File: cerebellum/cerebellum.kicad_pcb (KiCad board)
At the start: 4 copper layers, 91.5 x 52 mm, 89 parts, among them J1 Power_IN, J10 Arm_R, J11 Light, J2 Power_Back, J3 GD_LINK, J4 GD_LINK, J5 Head, J7 Leg_L, J8 Leg_R, J9 Arm_L, Q1 AP2300, Q2 FH1404G6, Q3 FH1404G6, Q4 FH1404G6, U1 GD32F405VGHx, U2 TPS5430DDAR, U3 BMI088, U4 TCAN4550RGYRQ1, U5 ICP-20100, Y1 8M, Y2 40M

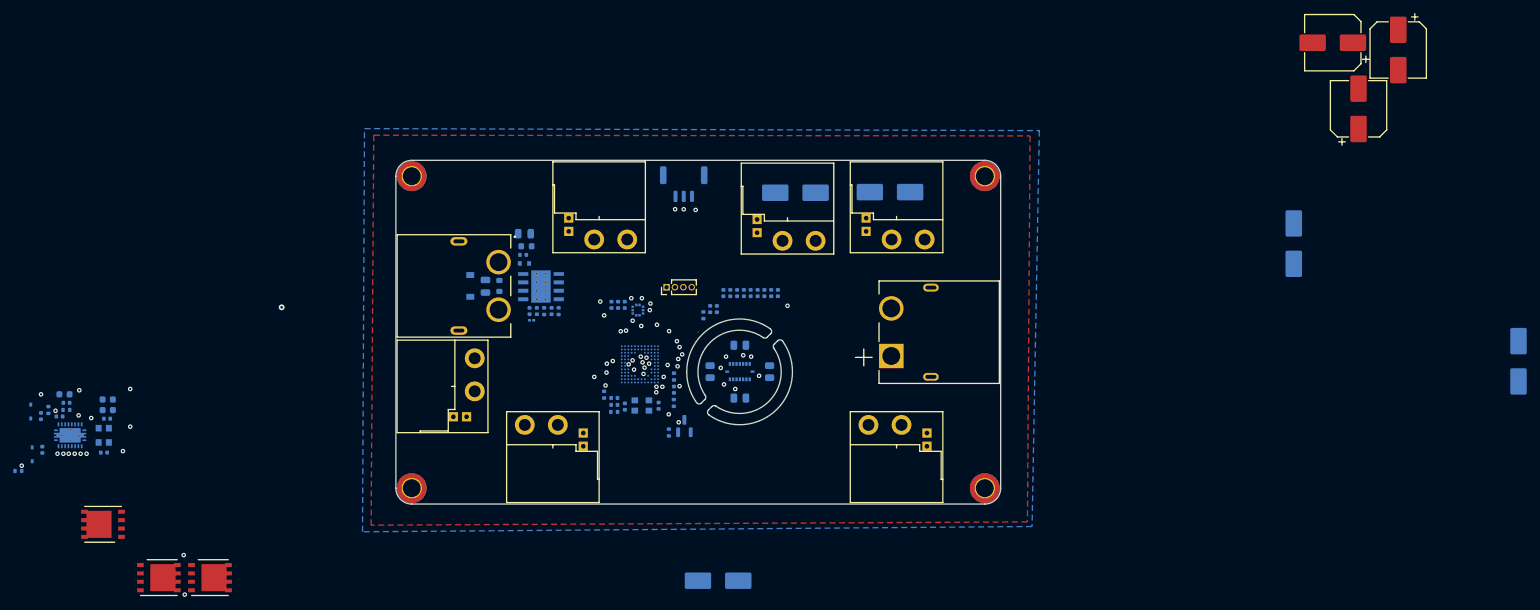
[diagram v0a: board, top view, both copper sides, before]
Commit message: [New] Refactoring placement & routing of cerebellum
Signed-off-by: Homalozoa <nx.tardis@gmail.com>
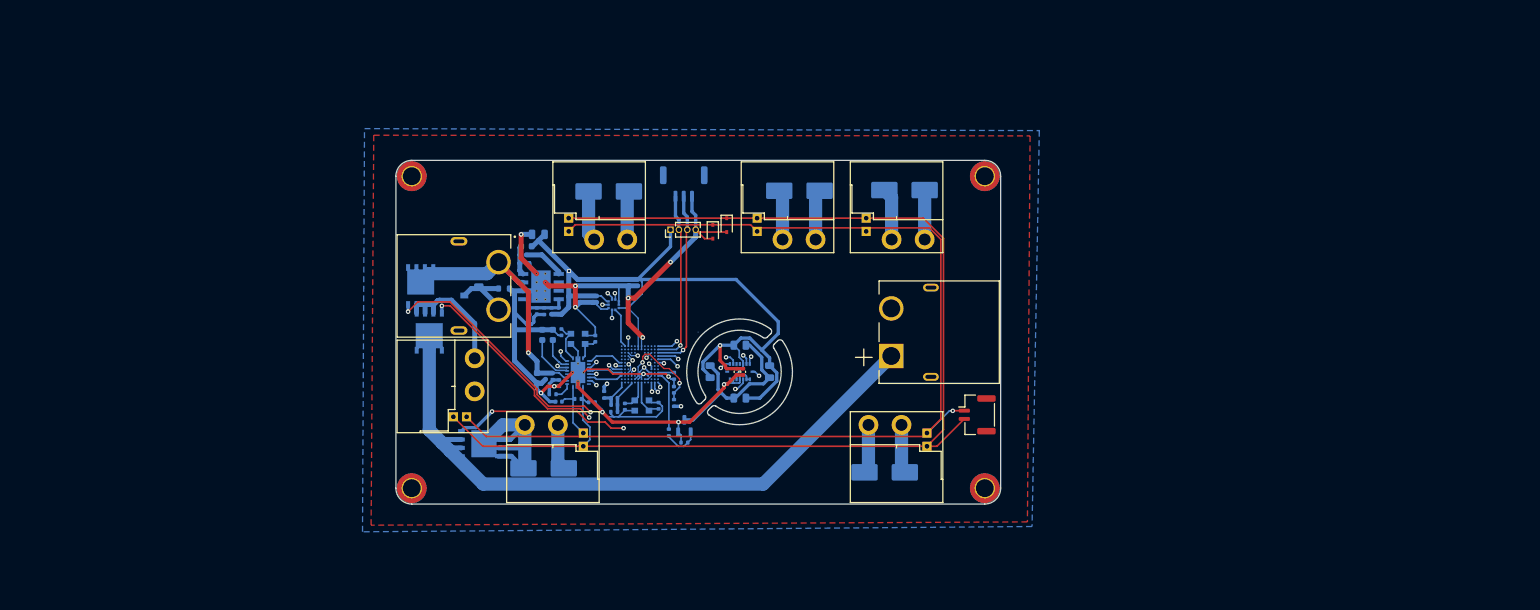
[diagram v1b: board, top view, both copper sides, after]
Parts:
- removed C36, C38, C40: 47uf, Capacitor_SMD:CP_Elec_8x6.2
- added J6: CAN, Connector_JST:JST_GH_BM02B-GHS-TBT_1x02-1MP_P1.25mm_Vertical, F.Cu at (192.2, 112.5)
- C29, C30, D3, D4: moved to F.Cu
- Q2, Q3, Q4: moved to B.Cu
- moved C35 148.4 mm to (126.6, 120.6), turned to 0 degrees
- moved D3 110.7 mm to (154.3, 83.8)
- moved D4 106.7 mm to (152.2, 84.8), turned to -90 degrees
- moved C37 104.0 mm to (136.4, 78.7), turned to 180 degrees
- moved R8 85.4 mm to (131.8, 110.1)
- moved C22 83.5 mm to (133.9, 110.6), turned to 180 degrees
- moved C23 78.4 mm to (128.9, 110.5), turned to 0 degrees
- moved U4 77.4 mm to (131.8, 106.1), turned to 180 degrees
- moved R4 76.3 mm to (128.0, 109.4), turned to 180 degrees
- moved C14 76.3 mm to (134.4, 101.0), turned to -90 degrees
- moved C16 75.8 mm to (128.9, 107.7), turned to 90 degrees
- moved R5 73.7 mm to (128.0, 106.7), turned to -90 degrees
- moved Y2 73.2 mm to (131.8, 101.0), turned to 90 degrees
- moved C25 72.6 mm to (126.9, 106.6), turned to -90 degrees
- moved C26 71.5 mm to (125.6, 107.0), turned to -90 degrees
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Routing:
- net GNDA: track 0.00 -> 250.5 mm
- net PWR_EXPORT: track 0.00 -> 242.4 mm
- net GND: track 0.00 -> 211.9 mm, vias 12 -> 13
- net CAN_L: track 0.00 -> 182.5 mm, vias 1 -> 0
- net CAN_H: track 0.00 -> 177.0 mm, vias 0 -> 1
- net +3V3: track 0.00 -> 174.6 mm, vias 5 -> 6
- net EXT_PWR: track 0.00 -> 100.6 mm
- net PWRCT_1: track 0.00 -> 54.9 mm, vias 1 -> 3
- net PWRCT_2: track 0.00 -> 49.7 mm, vias 1 -> 3
- net +24V: track 0.00 -> 42.0 mm
- net PWRCT_3: track 0.00 -> 40.7 mm
- net BMI_SDO: track 0.00 -> 39.9 mm
- net BMI_SDI: track 0.00 -> 32.4 mm
- net ACC_SCS: track 0.00 -> 32.3 mm
- net SWCLK: track 0.00 -> 27.7 mm, vias 2 -> 1
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
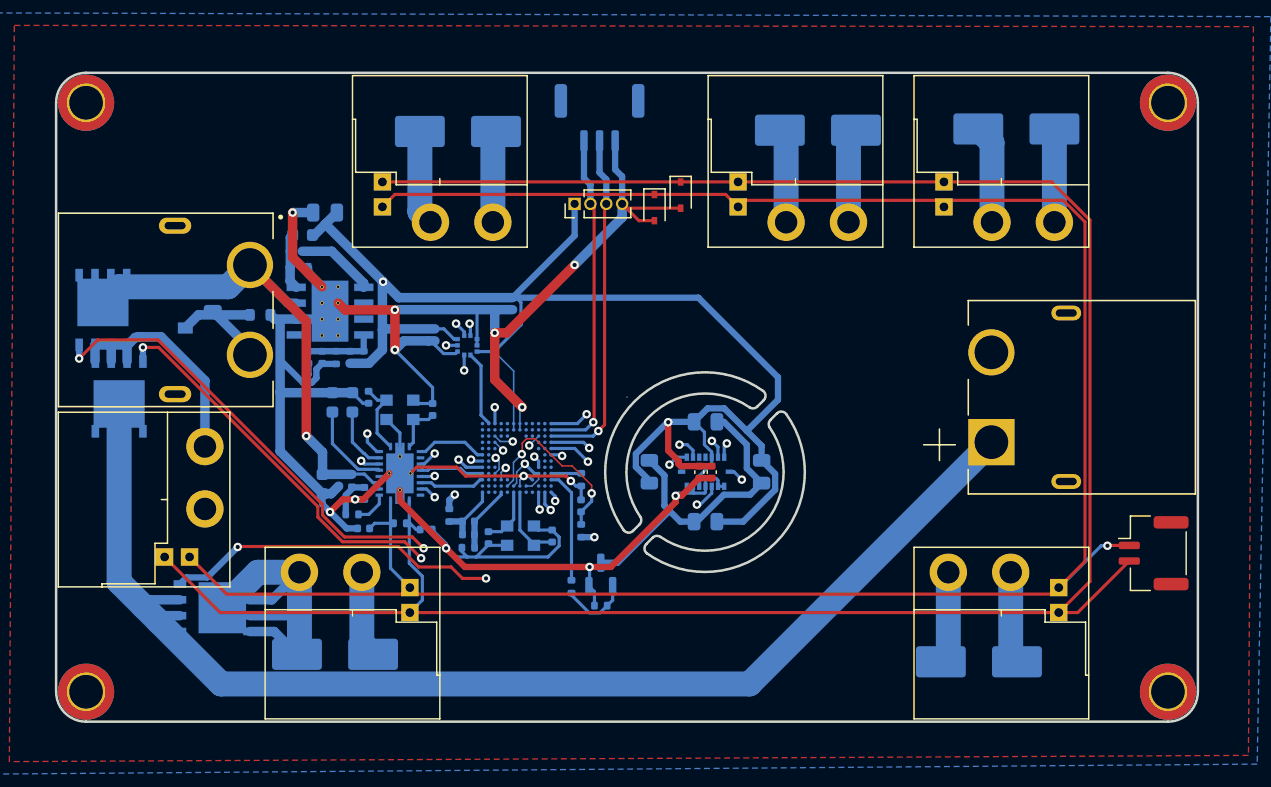
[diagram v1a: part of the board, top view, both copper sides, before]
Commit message: [New] Complete new cerebellum
1. it's based on NXP MIMXRT1061CVL5A
2. it supports xt30(2+2)x7 output, xt60x1 input
3. it supports CAN FD & CAN 2.0

Signed-off-by: Homalozoa <nx.tardis@gmail.com>
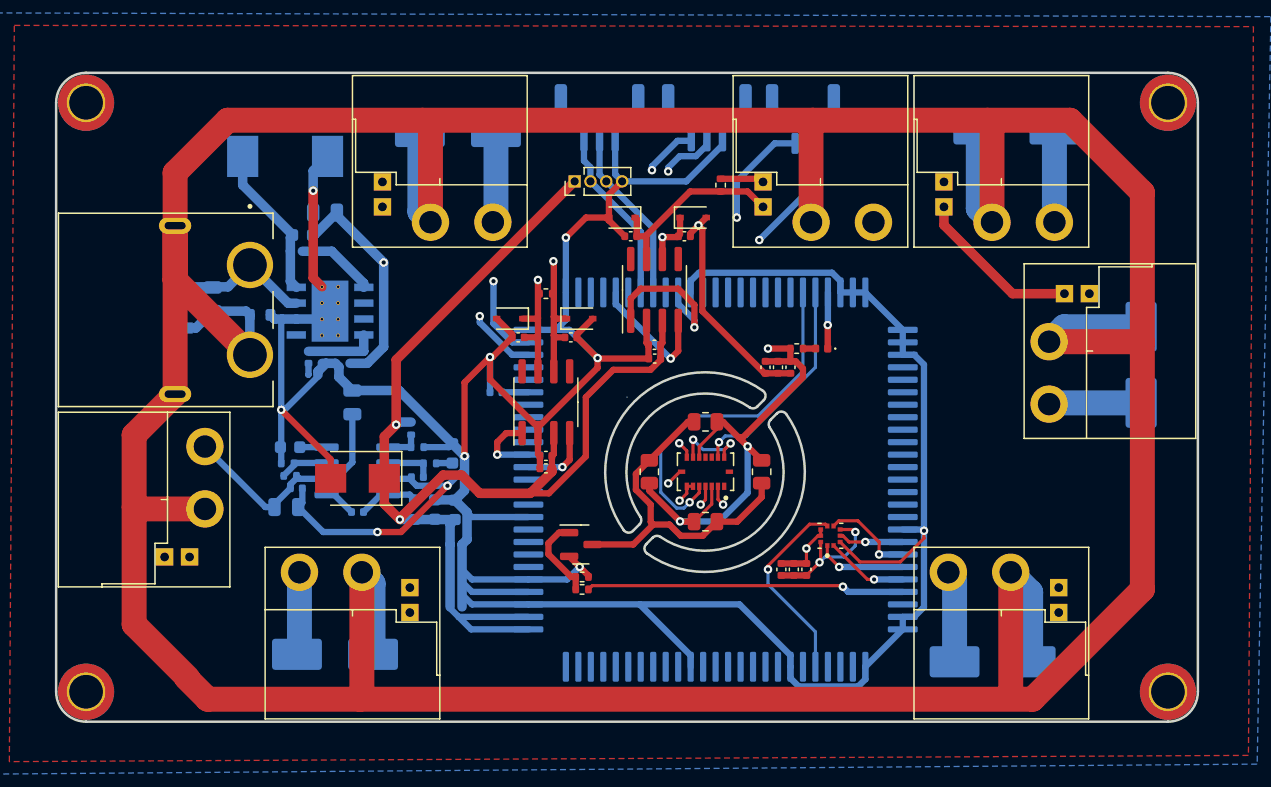
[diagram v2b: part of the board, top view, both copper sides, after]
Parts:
- removed Q2, Q3, Q4: FH1404G6, Rolling_Custom:PDFN5X6-8L
- removed Y1: 8M, Oscillator:Oscillator_SMD_EuroQuartz_XO32-4Pin_3.2x2.5mm
- removed Y2: 40M, Oscillator:Oscillator_SMD_EuroQuartz_XO32-4Pin_3.2x2.5mm
- added C36: 47uf 50V, Capacitor_SMD:C_0603_1608Metric, B.Cu at (136.2, 109.0)
- added C38: 100nF, 10%, 10V, Capacitor_SMD:C_0402_1005Metric, B.Cu at (139.5, 99.6)
- added D5: LTST-C281KFKT-5A, LED_SMD:LED_0402_1005Metric, F.Cu at (165.6, 96.1)
- added D6: 12V, Diode_SMD:D_SOD-323, F.Cu at (155.3, 85.6)
- added D7: 12V, Diode_SMD:D_SOD-323, F.Cu at (149.6, 85.6)
- added D8: B240, Diode_SMD:D_SMB, F.Cu at (128.4, 106.5)
- added J12: Back, Rolling_Custom:XT30PW(2+2), F.Cu at (183.8, 96.3)
- added R16: 10.2k, Resistor_SMD:R_0402_1005Metric, B.Cu at (132.7, 102.5)
- added R17: 1.96k, Resistor_SMD:R_0402_1005Metric, B.Cu at (133.2, 104.0)
- added U6: TJA1042T, Package_SO:SOIC-8_3.9x4.9mm_P1.27mm, F.Cu at (152.2, 91.4)
- added U7: TPS54231, Package_SO:SOIC-8_3.9x4.9mm_P1.27mm, B.Cu at (128.4, 105.9)
- C1: value 20pF, 10%, 10V -> 100nF, 10%, 10V
- C10, C20, C22, C23, C31, C32, C51, Q1, R10, R12, R13, R14, R15, R8, R9, U3, U5: moved to F.Cu
- C11, C9: value 10uF, 10%, 10V -> 100pF, 10%, 10V; moved to F.Cu
- C12, C8: value 100nF, 10%, 10V -> 4.7uF, 10%, 10V; moved to F.Cu
- C14: value 8.2pF, 10%, 50V -> 10pf 50V
- C15: value 8.2pF, 10%, 50V -> 1.5nf 50V; footprint Capacitor_SMD:C_0402_1005Metric -> Capacitor_SMD:C_0603_1608Metric
- C16: value 10nF, 10%, 50V -> 4.7uF 50V; footprint Capacitor_SMD:C_0402_1005Metric -> Capacitor_SMD:C_0805_2012Metric
- C18: value 470nF, 10%, 50V -> 4.7uF 50V; footprint Capacitor_SMD:C_0603_1608Metric -> Capacitor_SMD:C_0805_2012Metric
- C25: value 100nF, 10%, 50V -> 10uf 50V
- C26: value 10uF, 10%, 50V -> 8.2nf 50V
- C27: value 10uF, 10%, 50V -> 100nF, 10%, 10V; footprint Capacitor_SMD:C_0603_1608Metric -> Capacitor_SMD:C_0402_1005Metric
- C3: value 20pF, 10%, 10V -> 4.7uF, 10%, 10V
- C33: value 10uF, 10%, 10V -> 47uf 50V; footprint Capacitor_SMD:C_0402_1005Metric -> Capacitor_SMD:C_0603_1608Metric
- C4: value 100nF, 10%, 10V -> 1uF, 10%, 10V
- C6: value 4.7uF, 10%, 10V -> 10uF, 10%, 10V
- C7: value 1uF, 10%, 10V -> 100nF, 10%, 10V; moved to F.Cu
- D2: footprint Diode_SMD:D_SOD-523 -> Diode_SMD:D_SMC
- J2: value Power_Back -> UART; footprint Rolling_Custom:AMASS_XT60PW-M -> Connector_JST:JST_GH_SM03B-GHS-TB_1x03-1MP_P1.25mm_Horizontal; moved to B.Cu
- J3: value GD_LINK -> SWD_DBG
- J4: value GD_LINK -> SWD_DBG_PIN
- J6: moved to B.Cu
- L1: value 20R -> 15uh; footprint Resistor_SMD:R_0402_1005Metric -> Inductor_SMD:L_0603_1608Metric
- R1: value 10k, 5% -> 1k; moved to F.Cu
- R2: value 10k, 5% -> 120R; moved to F.Cu
- R3: value 0 -> 64.9k
- R4: value 33k -> 169k
- R5: value 3k -> 20.5
- U1: value GD32F405VGHx -> OK1061-S; footprint Rolling_Custom:Modified-BGA-100_7x7mm_Layout12x12_P0.5mm -> Rolling_Custom:OK1061-S-100
- U4: value TCAN4550RGYRQ1 -> TJA1042T; footprint Rolling_Custom:VQFN20 -> Package_SO:SOIC-8_3.9x4.9mm_P1.27mm; moved to F.Cu
- moved J6 44.7 mm to (164.1, 77.7), turned to 180 degrees
- moved J2 36.5 mm to (156.4, 77.6), turned to 0 degrees
- moved C32 35.2 mm to (163.4, 113.8), turned to 90 degrees
- moved C51 35.2 mm to (162.4, 113.8), turned to 90 degrees
- moved C31 35.2 mm to (164.4, 113.8), turned to 90 degrees
- moved U5 32.9 mm to (166.3, 111.1)
- moved C39 32.0 mm to (191.2, 97.4), turned to 90 degrees
- moved C20 27.9 mm to (163.1, 97.6)
- moved C11 26.3 mm to (150.3, 87.1), turned to 0 degrees
- moved R2 26.1 mm to (157.5, 83.0), turned to 90 degrees
- moved C6 24.4 mm to (136.3, 116.8), turned to 0 degrees
- moved R1 22.6 mm to (163.6, 96.1), turned to 180 degrees
- moved R8 21.8 mm to (143.5, 91.7)
- moved C4 20.6 mm to (136.3, 112.8), turned to 0 degrees
- moved C23 19.7 mm to (141.3, 95.2)
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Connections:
- C1 pad 1: GND -> +5V
- C1 pad 2: MCU_OSC_IN -> GND
- C10 pad 1: GND -> +5V
- C10 pad 2: +3V3 -> GND
- C11 pad 1: VREF_S -> GND
- C11 pad 2: VREF_D -> CANFD_H
- C12 pad 1: VREF_S -> +5V
- C12 pad 2: VREF_D -> GND
- C14 pad 1: GND -> 5V_CMP
- C14 pad 2: TCAN_OSC_IN -> GND
- C15 pad 1: GND -> Net-(C15-Pad1)
- C15 pad 2: TCAN_OSC_OUT -> GND
- C16 pad 1: GND -> +24V
- C16 pad 2: Net-(C16-Pad2) -> GND
- C18 pad 1: Net-(C18-Pad1) -> +24V
- C2 pad 1: NRST -> +5V
- C26 pad 1: +24V -> Net-(C26-Pad1)
- C27 pad 1: VCCOUT -> Net-(C27-Pad1)
- C27 pad 2: GND -> Net-(C27-Pad2)
- C3 pad 1: GND -> +5V
- C3 pad 2: MCU_OSC_OUT -> GND
- C33 pad 1: +3V3 -> +5V
- C34 pad 1: PWR_EXPORT -> +24V
- C35 pad 1: PWR_EXPORT -> +24V
- C37 pad 1: PWR_EXPORT -> +24V
- C39 pad 1: PWR_EXPORT -> +24V
- C4 pad 1: +3V3 -> +5V
- C41 pad 1: PWR_EXPORT -> +24V
- C5 pad 1: +3V3 -> +5V
- C6 pad 1: +3V3 -> +5V
- C7 pad 1: +3V3 -> +5V
- C8 pad 1: +3V3 -> +5V
- C9 pad 2: +3V3 -> CANFD_L
- J10 pad 1: PWR_EXPORT -> +24V
- J10 pad 3: CAN_H -> CANFD_H
- J10 pad 4: CAN_L -> CANFD_L
- J11 pad 1: PWR_EXPORT -> +24V
- J11 pad 3: CAN_H -> CANFD_H
- J11 pad 4: CAN_L -> CANFD_L
- J2 pad 1: EXT_PWR -> UART_TX
- J2 pad 2: GNDA -> UART_RX
- J3 pad 1: +3V3 -> +5V
- J5 pad 1: PWR_EXPORT -> +24V
- J5 pad 3: CAN_H -> CANFD_H
- J5 pad 4: CAN_L -> CANFD_L
- J7 pad 1: PWR_EXPORT -> +24V
- J7 pad 3: CAN_H -> CANFD_H
- J7 pad 4: CAN_L -> CANFD_L
- J8 pad 1: PWR_EXPORT -> +24V
- J8 pad 3: CAN_H -> CANFD_H
- J8 pad 4: CAN_L -> CANFD_L
- J9 pad 1: PWR_EXPORT -> +24V
- J9 pad 3: CAN_H -> CANFD_H
- J9 pad 4: CAN_L -> CANFD_L
- L1 pad 1: +3V3 -> +5V
- L1 pad 2: VREF_D -> Net-(C27-Pad1)
- R1 pad 1: +3V3 -> Net-(D5-Pad2)
- R1 pad 2: NRST -> +3V3
- R2 pad 1: Net-(R2-Pad1) -> CANFD_H
- R2 pad 2: GND -> CANFD_L
- R3 pad 1: GND -> 5V_CMP
- R3 pad 2: VREF_S -> Net-(C15-Pad1)
- R4 pad 1: TCAN_WAKE -> +24V
- R4 pad 2: Net-(C16-Pad2) -> Net-(R4-Pad2)
- R5 pad 1: +24V -> Net-(R4-Pad2)
- R5 pad 2: Net-(C16-Pad2) -> GND
- U3 pad 10: BMI_SDO -> SENSOR_SDO
- U3 pad 15: BMI_SDO -> SENSOR_SDO
- U3 pad 8: BMI_SCK -> SENSOR_SCK
- U3 pad 9: BMI_SDI -> SENSOR_SDI
- U4 pad 1: TCAN_OSC_IN -> CAN_TX
- U4 pad 2: TCAN_WKRQ -> GND
- U4 pad 3: unconnected-(U4-Pad3) -> +5V
- U4 pad 4: TCAN_SCK -> CAN_RX
- U4 pad 5: TCAN_SDI -> unconnected-(U4-Pad5)
- U4 pad 6: TCAN_SDO -> CAN_L
- U4 pad 7: TCAN_SCS -> CAN_H
- U4 pad 8: TCAN_INT -> unconnected-(U4-Pad8)
- U5 pad 2: ICP_SCK -> SENSOR_SCK
- U5 pad 4: ICP_SDI -> SENSOR_SDI
- U5 pad 6: ICP_SDO -> SENSOR_SDO
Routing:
- net +24V: track 42.0 -> 375.6 mm, vias 1 -> 0
- net PWR_EXPORT: track 242.4 -> 0.00 mm
- net CANFD_L: track 0.00 -> 184.1 mm, vias 0 -> 1
- net CANFD_H: track 0.00 -> 170.8 mm
- net GND: track 211.9 -> 375.1 mm, vias 13 -> 15
- net CAN_L: track 182.5 -> 35.9 mm, vias 0 -> 2
- net CAN_H: track 177.0 -> 38.2 mm, vias 1 -> 2
- net GNDA: track 250.5 -> 354.3 mm
- net EXT_PWR: track 100.6 -> 0.00 mm
- net +5V: track 0.00 -> 98.5 mm, vias 0 -> 2
- net PWRCT_1: track 54.9 -> 0.00 mm, vias 3 -> 0
- net PWRCT_2: track 49.7 -> 0.00 mm, vias 3 -> 0
- net +3V3: track 174.6 -> 126.2 mm
- net PWRCT_3: track 40.7 -> 0.00 mm, vias 3 -> 0
- net BMI_SDO: track 39.9 -> 0.00 mm, vias 3 -> 0
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- added copper zone on In1.Cu, net +24V
- added copper zone on In2.Cu, net +5V
- removed copper zone on In2.Cu, net +3V3
- removed copper zone on In1.Cu, net EXT_PWR

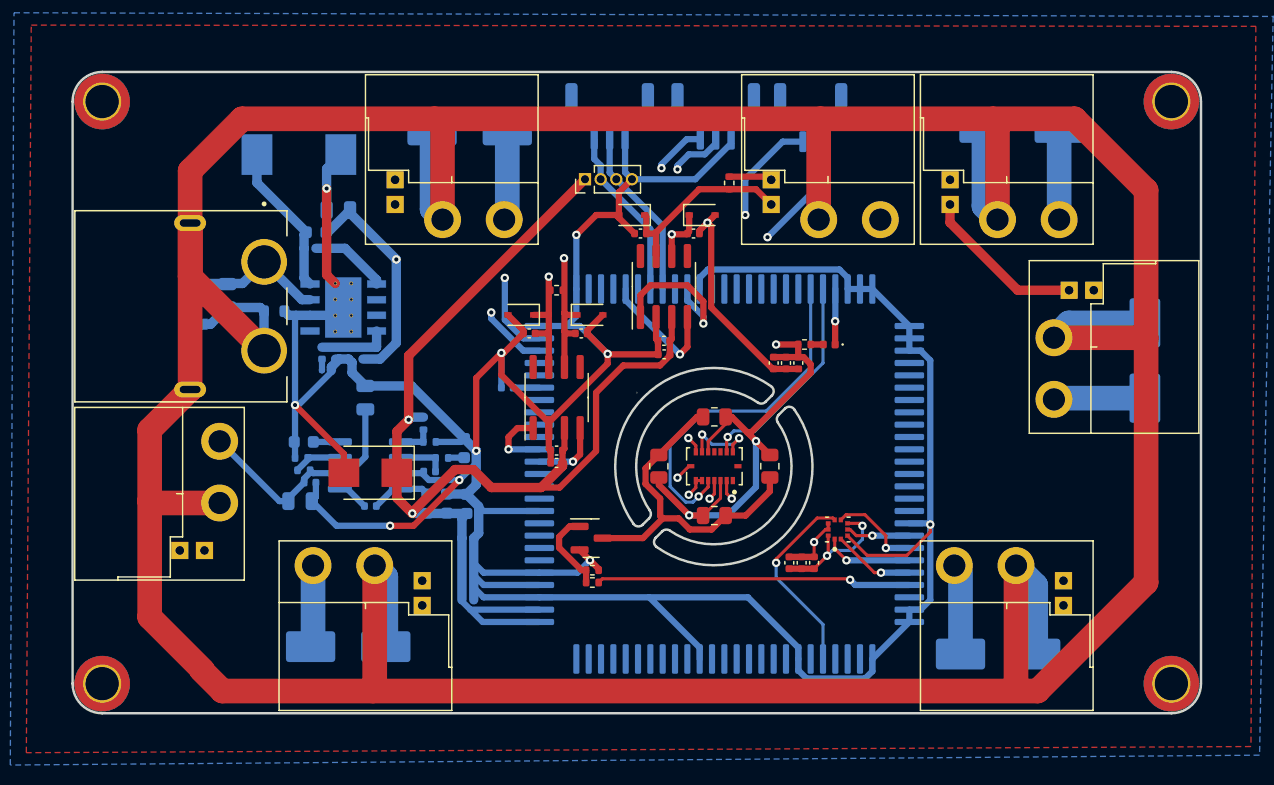
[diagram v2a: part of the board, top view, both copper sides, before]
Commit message: [Update] Redesign PCB layout of cerebellum
1. Remove duplicated xt30(2+2) ports
2. Redesign PCB layout for new cerebellum
3. Add lines in cerebellum schematic to split different functional area.
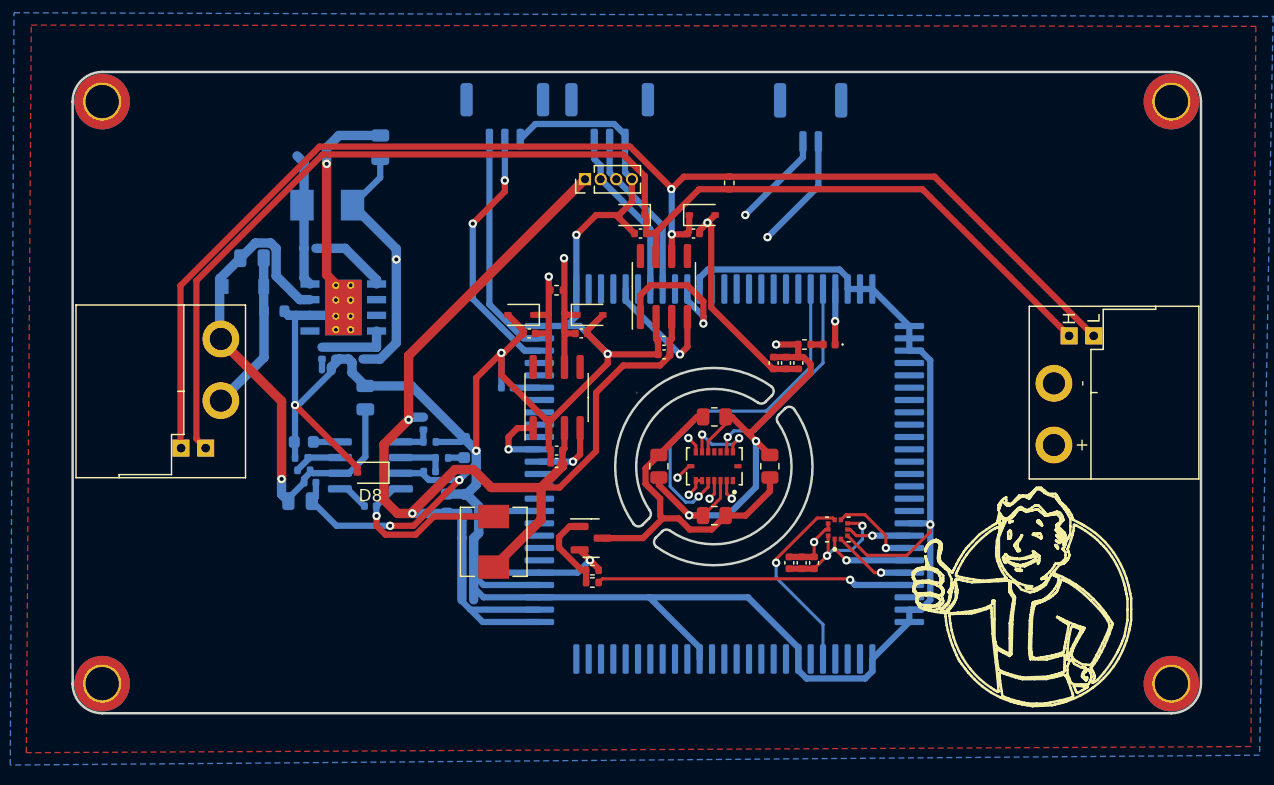
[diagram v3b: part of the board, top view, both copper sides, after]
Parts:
- removed C34, C35, C37, C39, C41: 47uf, Capacitor_SMD:CP_Elec_8x6.2
- removed J10: Arm_R, Rolling_Custom:XT30PW(2+2)
- removed J11: Light, Rolling_Custom:XT30PW(2+2)
- removed J12: Back, Rolling_Custom:XT30PW(2+2)
- removed J7: Leg_L, Rolling_Custom:XT30PW(2+2)
- removed J8: Leg_R, Rolling_Custom:XT30PW(2+2)
- removed J9: Arm_L, Rolling_Custom:XT30PW(2+2)
- D2: value ESD5Z3V3 -> BZT52C3V3S; footprint Diode_SMD:D_SMC -> Diode_SMD:D_SOD-323
- D8: value B240 -> BZT52C5V1S; footprint Diode_SMD:D_SMB -> Diode_SMD:D_SOD-323
- J1: value Power_IN -> PowerIn; footprint Rolling_Custom:AMASS_XT60PW-F -> Rolling_Custom:XT30PW(2+2)
- J5: value Head -> PowerOut
- L1: value 15uh -> 15uh, SLO0530H150MTT; footprint Inductor_SMD:L_0603_1608Metric -> Inductor_SMD:L_Sunlord_MWSA0518_5.4x5.2mm; moved to F.Cu
- L2: value 15uh -> 15uh, SLO0530H150MTT; footprint Inductor_SMD:L_0603_1608Metric -> Inductor_SMD:L_Sunlord_MWSA0518_5.4x5.2mm
- U2: value TPS5430DDAR -> TPS5430DDA; footprint Rolling_Custom:TPS5430DDAR -> Package_SO:TI_SO-PowerPAD-8_ThermalVias
- moved J1 64.4 mm to (183.8, 100.0), turned to 90 degrees
- moved J2 17.1 mm to (139.3, 77.6)
- moved J5 8.30 mm to (116.3, 99.9)
- moved L1 6.23 mm to (138.4, 112.1)
- moved C19 6.13 mm to (129.2, 80.1), turned to -90 degrees
- moved D1 3.77 mm to (118.1, 91.4), turned to 180 degrees
- moved C13 3.65 mm to (118.8, 89.1), turned to 0 degrees
- moved L2 2.38 mm to (124.9, 84.8)
- moved D2 0.91 mm to (123.5, 80.8)
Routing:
- net GNDA: track 354.3 -> 107.0 mm
- net +24V: track 375.6 -> 149.8 mm, vias 0 -> 1
- net CANFD_L: track 184.1 -> 107.2 mm, vias 1 -> 2
- net CANFD_H: track 170.8 -> 102.4 mm
- net UART_TX: track 29.2 -> 18.6 mm, vias 2 -> 0
- net UART_RX: track 31.5 -> 21.2 mm
- net Net-(C27-Pad1): track 4.87 -> 14.6 mm, vias 0 -> 1
- net +5V: track 98.5 -> 108.1 mm
- net GND: track 375.1 -> 378.8 mm
- net +3V3: track 126.2 -> 128.5 mm
- net Net-(C17-Pad2): track 12.4 -> 10.8 mm
- net CAN_L: track 35.9 -> 34.9 mm
- added copper zone on In1.Cu, net +3V3
- removed copper zone on In1.Cu, net +24V
